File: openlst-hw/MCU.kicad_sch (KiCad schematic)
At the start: 39 parts, among them J1 Conn_02x03_Pin, J2 Conn_01x06_Pin, J3 Conn_01x03_Pin, J4 Conn_01x03_Pin, U1 CC1110, U2 MIC803, X1 27MHz

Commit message: propate the changes to RF
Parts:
- C1, C10, C11, C12, C14, C2, C3, C4, C5, C7, C8: Order https://www.digikey.com/product-detail/en/samsung-electro-m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 -> (none)
- C13: Order https://www.digikey.com/en/products/detail/samsung-electro-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 -> (none)
- D1, D2: Order https://www.digikey.com/product-detail/en/w%C3%BCrth-elektr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 -> (none)
- FB1: Order https://www.digikey.com/en/products/detail/murata-electroni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 -> (none)
- J1: Order https://www.digikey.com/en/products/detail/adam-tech/HPH2-A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 -> (none); Part Number (none) -> generic; now fitted
- J2, J3, J4: Part Number (none) -> generic; now fitted
- R1, R14: Order https://www.digikey.com/product-detail/en/bourns-inc/CR0603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 -> (none)
- R10, R11, R15, R2, R3, R5, R6, R7: Order https://www.digikey.com/en/products/detail/stackpole-electr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 -> (none)
- R4: Order https://www.digikey.com/en/products/detail/yageo/RC0603JR-0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 -> (none)
- U2: Order https://www.digikey.com/en/products/detail/microchip-techno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 -> (none)
- X1: Order https://www.digikey.com/en/products/detail/epson/TG2520SMN-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 -> (none)

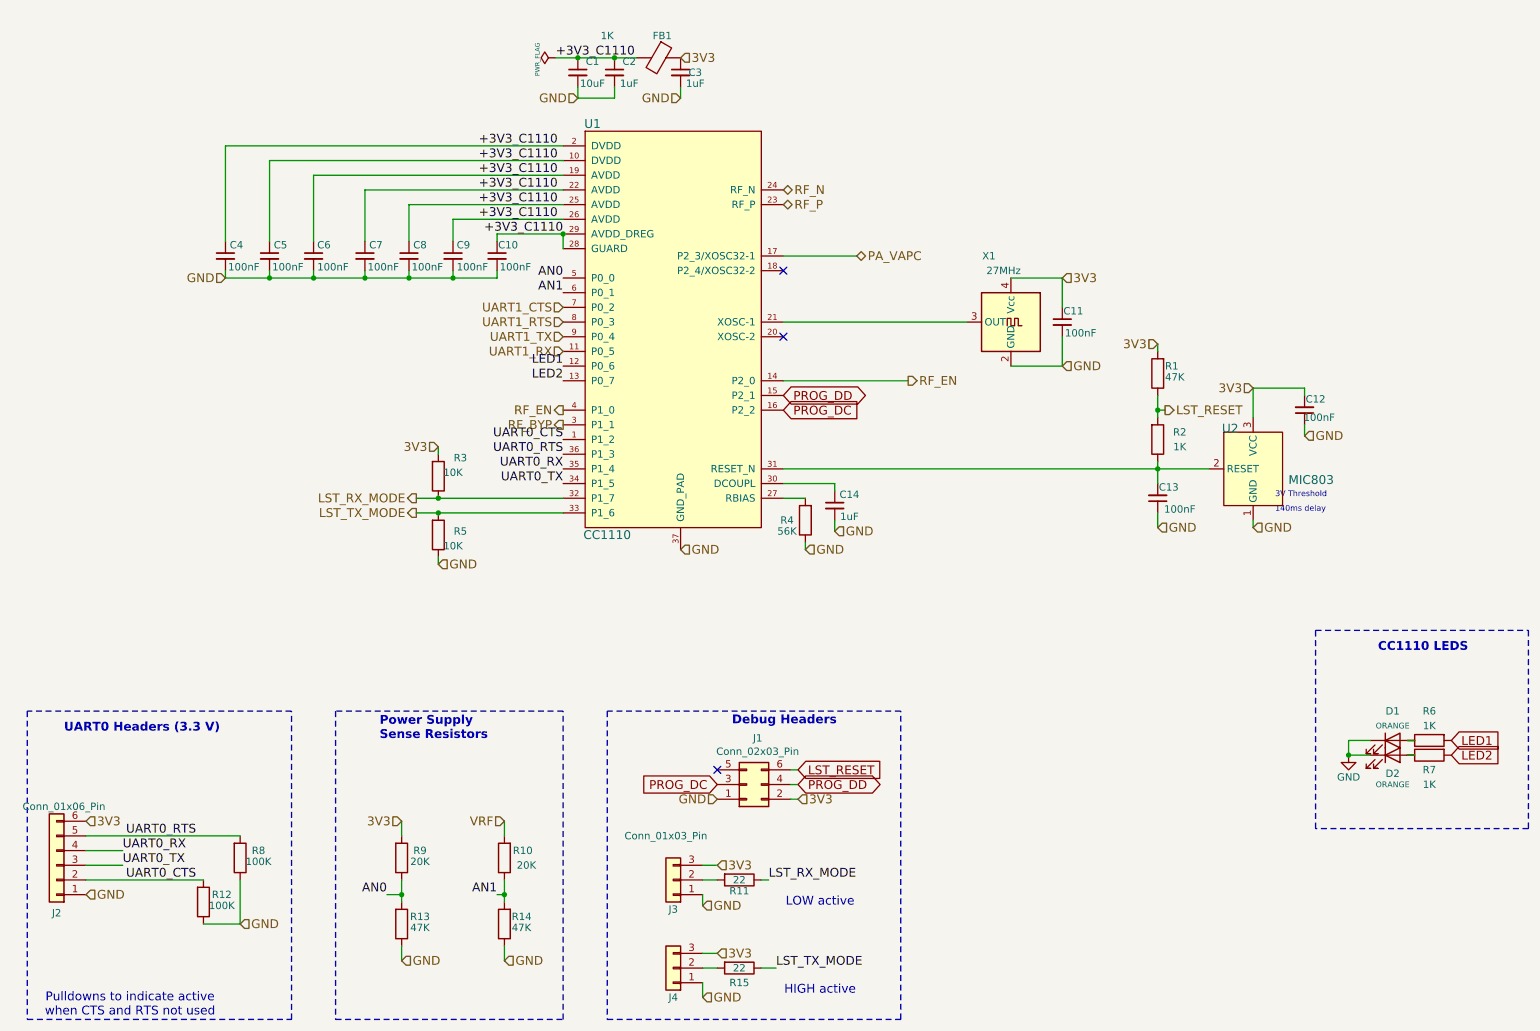
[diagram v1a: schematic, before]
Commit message: local switches and monitors for SCI and RF
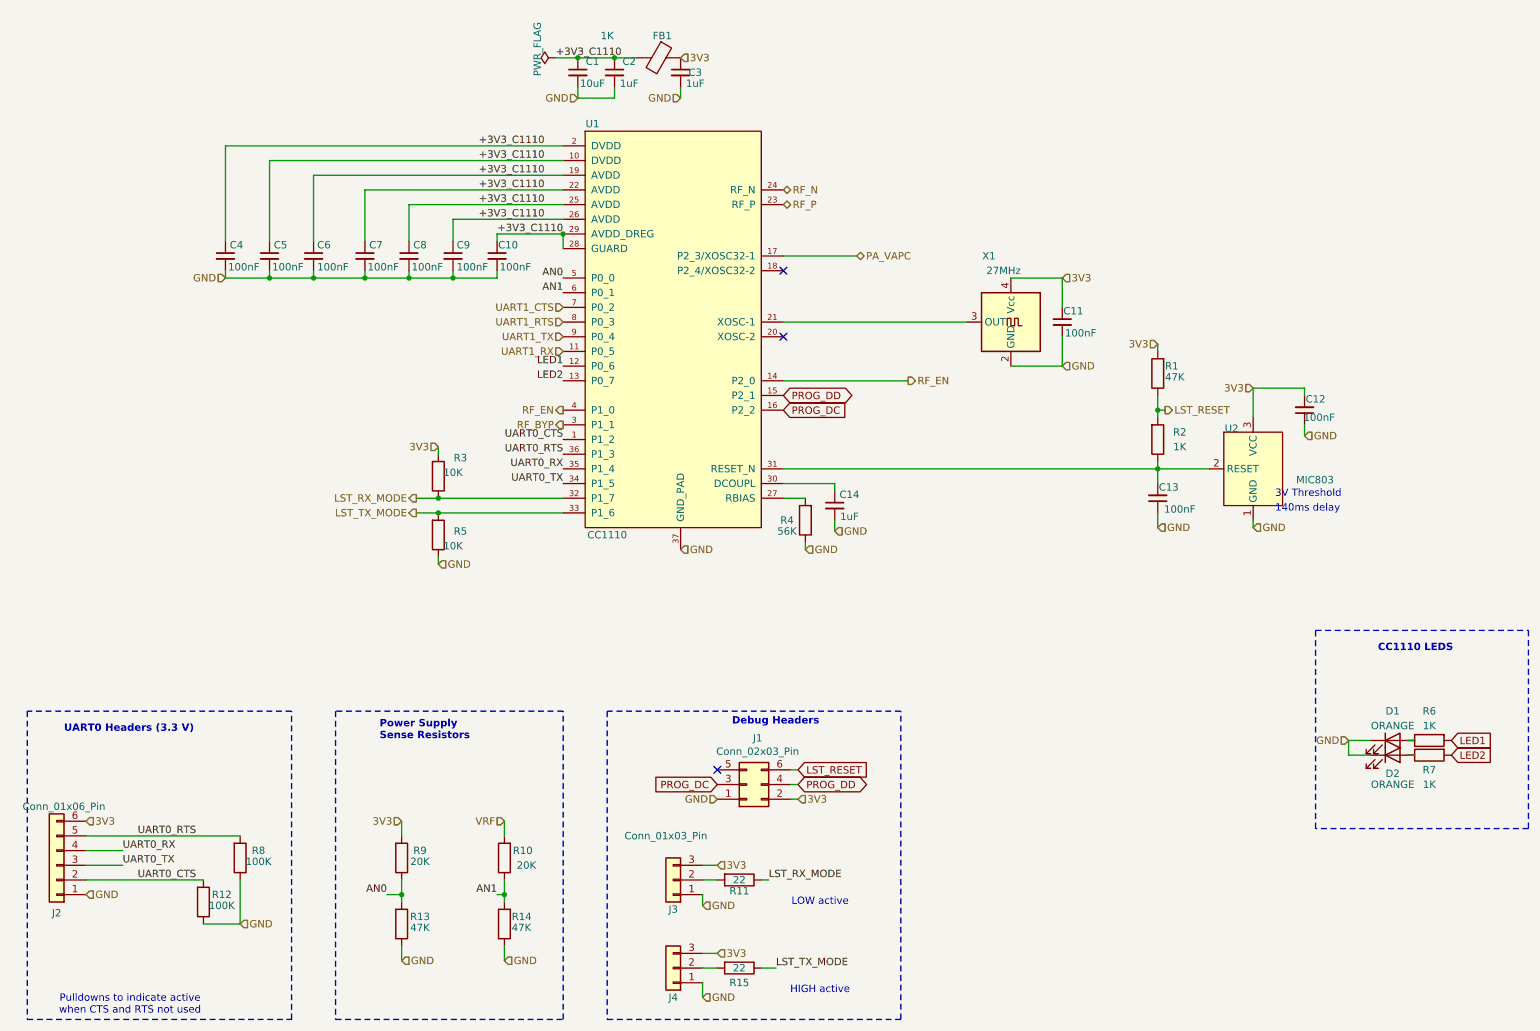
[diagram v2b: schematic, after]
